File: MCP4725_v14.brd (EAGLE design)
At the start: 15.2 x 14 mm, 15 parts

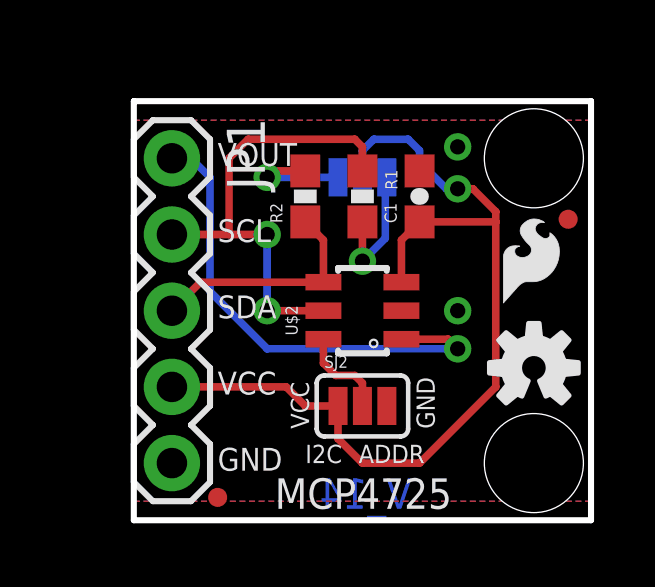
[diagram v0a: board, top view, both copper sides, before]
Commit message: Addressed issues from first review
added new jumper packages
moved and rerouted to avoid cutting of silk text
added extra GND pad for VOUT
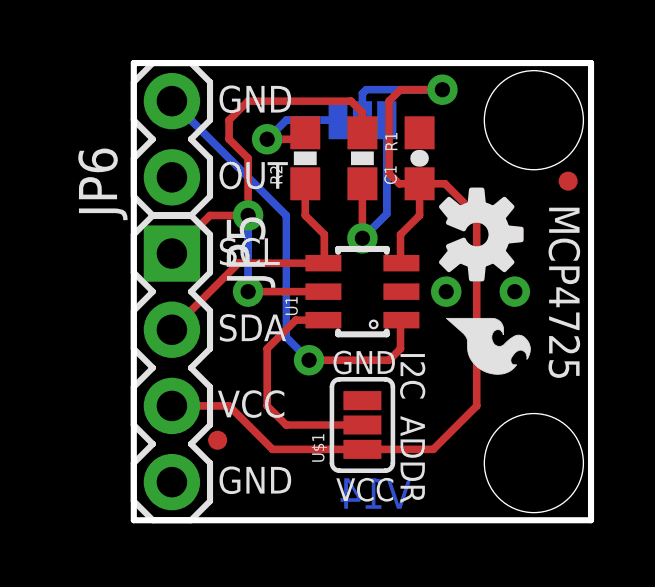
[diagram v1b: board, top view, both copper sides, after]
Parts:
- removed JP1: (no value), SparkFun:1X05
- removed SJ2: (no value), SparkFun-Passives:SJ_3_PASTE2&3
- removed U$2: DAC_MCP4725SOT-CP, SparkFun-AnalogIC:SOT23-6-MCP4725
- added GND: LOGO-SFESK, SparkFun:SFE-LOGO-FLAME
- added JP5: (no value), SparkFun-Connectors:1X04
- added JP6: M02PTH, SparkFun-Connectors:1X02
- added U1: DAC_MCP4725SOT-CP, SparkFun-AnalogIC:SOT23-6-MCP4725
- SJ1: device SparkFun-Passives:SJ_3_PASTE1&2&3 -> SparkFun-Passives:PAD-JUMPER-3-3OF3_NC_BY_TRACE_YES_SILK_FULL_BOX
- U$1: value LOGO-SFESK -> (none); device SparkFun:SFE-LOGO-FLAME -> SparkFun-Passives:PAD-JUMPER-3-2OF3_NC_BY_PASTE_YES_SILK_FULL_BOX
- moved U$1 6.21 mm to (7.62, 3.17), turned to 90 degrees
- moved LOGO1 4.84 mm to (11.4, 9.53), turned to 270 degrees
- moved SJ1 1.91 mm to (7.62, 13.3)
- moved JP2 1.90 mm to (2.79, 2.67)
- moved U$3 1.42 mm to (10.2, 3.17)
- moved JP3 1.27 mm to (14.5, 11.3)
- moved STANDOFF1 1.27 mm to (13.3, 13.3)
- moved C1 1.27 mm to (9.53, 12.1)
- moved R1 1.27 mm to (7.62, 12.1)
- moved R2 1.27 mm to (5.71, 12.1)
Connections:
- net GND: now also JP5.4, JP6.1, U$1.3, U1.2; no longer JP1.5, SJ2.3, U$2.2
- net N$3: now also U$1.2, U1.4; no longer SJ2.2, U$2.4
- net SCL: now also JP5.1, U1.5; no longer JP1.2, U$2.5
- net SDA: now also JP5.2, U1.6; no longer JP1.3, U$2.6
- net VCC: now also JP5.3, U$1.1, U1.1; no longer JP1.4, SJ2.1, U$2.1
- net VOUT: now also JP6.2, U1.3; no longer JP1.1, U$2.3
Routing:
- net N$3: track 3.14 -> 7.61 mm
- net VOUT: track 16.4 -> 14.7 mm
- net N$2: track 4.44 -> 6.09 mm
- net SCL: track 15.7 -> 17.1 mm
- net VCC: track 30.9 -> 32.1 mm
- net SDA: track 7.70 -> 8.89 mm
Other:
- board size 15.2 x 14 mm -> 15.2 x 15.2 mm
- board text added: "OUT"
- board text added: "V14"
- board text removed: "VOUT"
- board text removed: "V_14"
